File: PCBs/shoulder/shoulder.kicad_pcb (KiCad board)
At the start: 2 copper layers, 88 x 88 mm, 4 parts

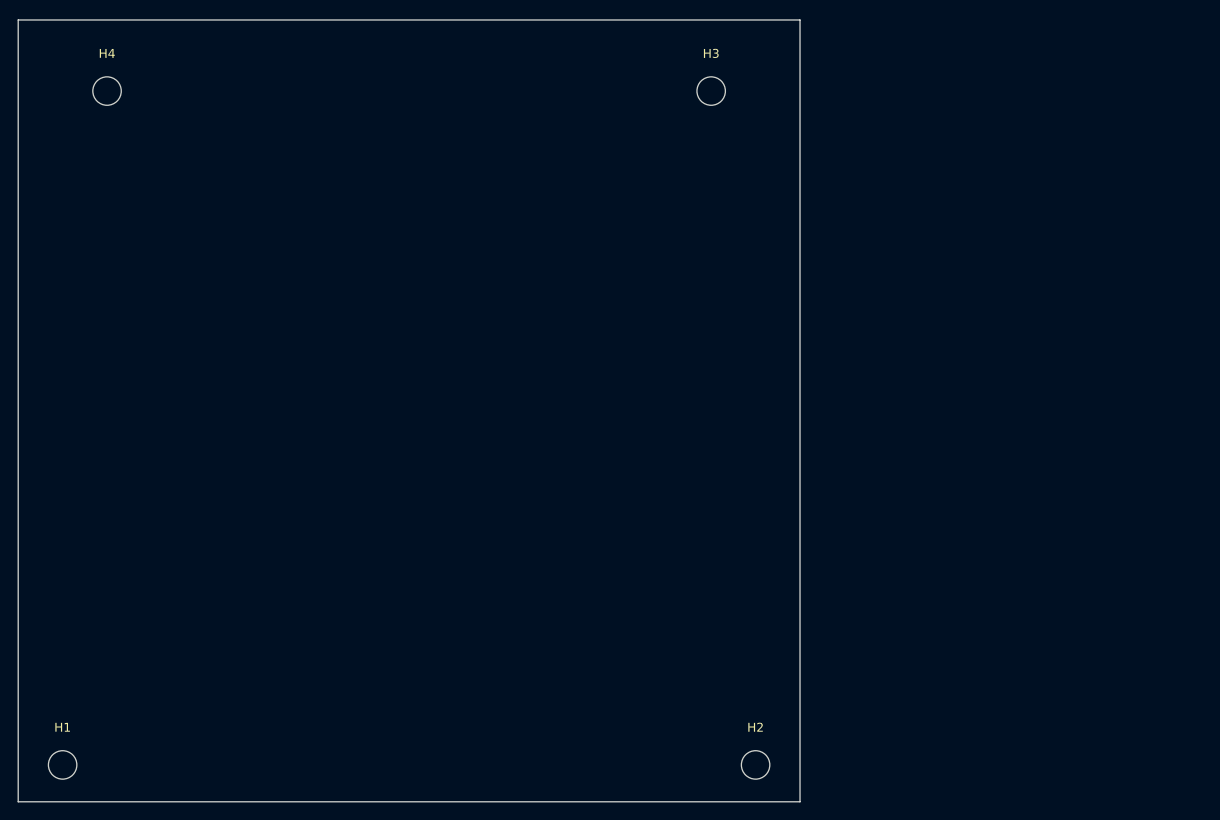
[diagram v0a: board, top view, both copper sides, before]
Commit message: Shoulder motor assy almost done. Need to find a library for the 2N551 NPN and redo the circuit. Ensure that the footprint pinout is correct
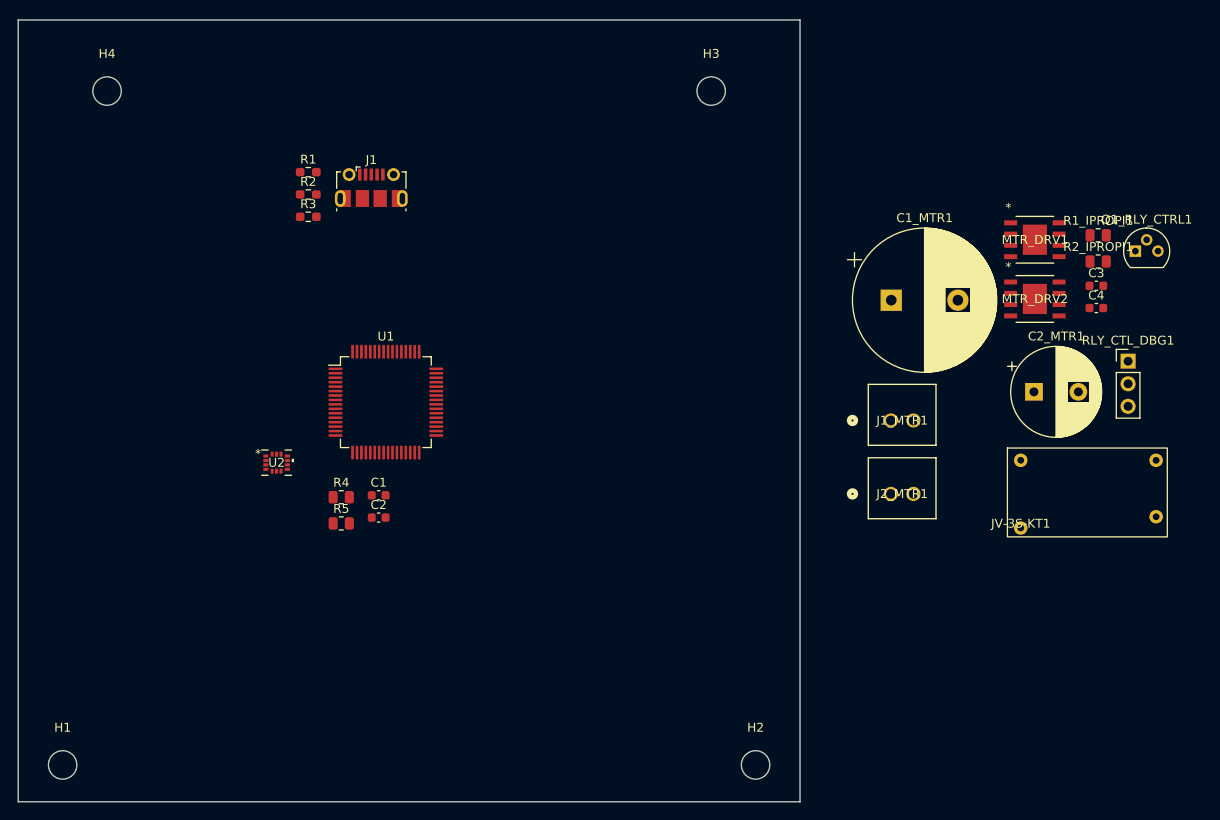
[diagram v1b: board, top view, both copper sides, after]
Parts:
- added C1: 100nF, Capacitor_SMD:C_0603_1608Metric, F.Cu at (97.1, 68.2)
- added C1_MTR1: 330muF, Capacitor_THT:CP_Radial_D16.0mm_P7.50mm, F.Cu at (154.8, 46.2)
- added C2: 100nF, Capacitor_SMD:C_0603_1608Metric, F.Cu at (97.1, 70.7)
- added C2_MTR1: 220muF, Capacitor_THT:CP_Radial_D10.0mm_P5.00mm, F.Cu at (170.9, 56.6)
- added C3: 100nF, Capacitor_SMD:C_0603_1608Metric, F.Cu at (177.9, 44.6)
- added C4: 100nF, Capacitor_SMD:C_0603_1608Metric, F.Cu at (177.9, 47.1)
- added J1: USB_B_Micro, Connector_USB:USB_Micro-B_Molex-105017-0001, F.Cu at (96.3, 33.6)
- added J1_MTR1: 705430001, 70543-0001:70543-0001_MOL, F.Cu at (154.8, 59.8)
- added J2_MTR1: 705430001, 70543-0001:70543-0001_MOL, F.Cu at (154.8, 68.0)
- added JV-3S-KT1: RELAY, JV-3S-KT:JV-3S-KT, F.Cu at (177.0, 66.8)
- added MTR_DRV1: DRV8251ADDAR, DRV8251A:SOIC8_DDA_TEX, F.Cu at (171.0, 39.4)
- added MTR_DRV2: DRV8251ADDAR, DRV8251A:SOIC8_DDA_TEX, F.Cu at (171.0, 46.1)
- added Q1_RLY_CTRL1: Q_NIGBT_CGE, Package_TO_SOT_THT:TO-92, F.Cu at (182.3, 40.7)
- added R1: 82k, Resistor_SMD:R_0603_1608Metric_Pad0.98x0.95mm_HandSolder, F.Cu at (89.2, 31.8)
- added R1_IPROPI1: 510Ohm, Resistor_SMD:R_0805_2012Metric, F.Cu at (178.1, 38.9)
- added R2: 33k, Resistor_SMD:R_0603_1608Metric_Pad0.98x0.95mm_HandSolder, F.Cu at (89.2, 34.3)
- added R2_IPROPI1: 510Ohm, Resistor_SMD:R_0805_2012Metric, F.Cu at (178.1, 41.9)
- added R3: 1k5, Resistor_SMD:R_0603_1608Metric_Pad0.98x0.95mm_HandSolder, F.Cu at (89.2, 36.9)
- added R4: 10k, Resistor_SMD:R_0805_2012Metric, F.Cu at (92.9, 68.4)
- added R5: 10k, Resistor_SMD:R_0805_2012Metric, F.Cu at (92.9, 71.4)
- added RLY_CTL_DBG1: Conn_01x03, Connector_PinHeader_2.54mm:PinHeader_1x03_P2.54mm_Vertical, F.Cu at (181.5, 53.1)
- added U1: STM32F303RETx, Package_QFP:LQFP-64_10x10mm_P0.5mm, F.Cu at (98.0, 57.7)
- added U2: LSM6DSMTR, LSM6DSMTR:LGA-14L_2P5X3X0P83_STM, F.Cu at (85.7, 64.5)

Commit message: Torso all but complete, making bogie before checking the last mark
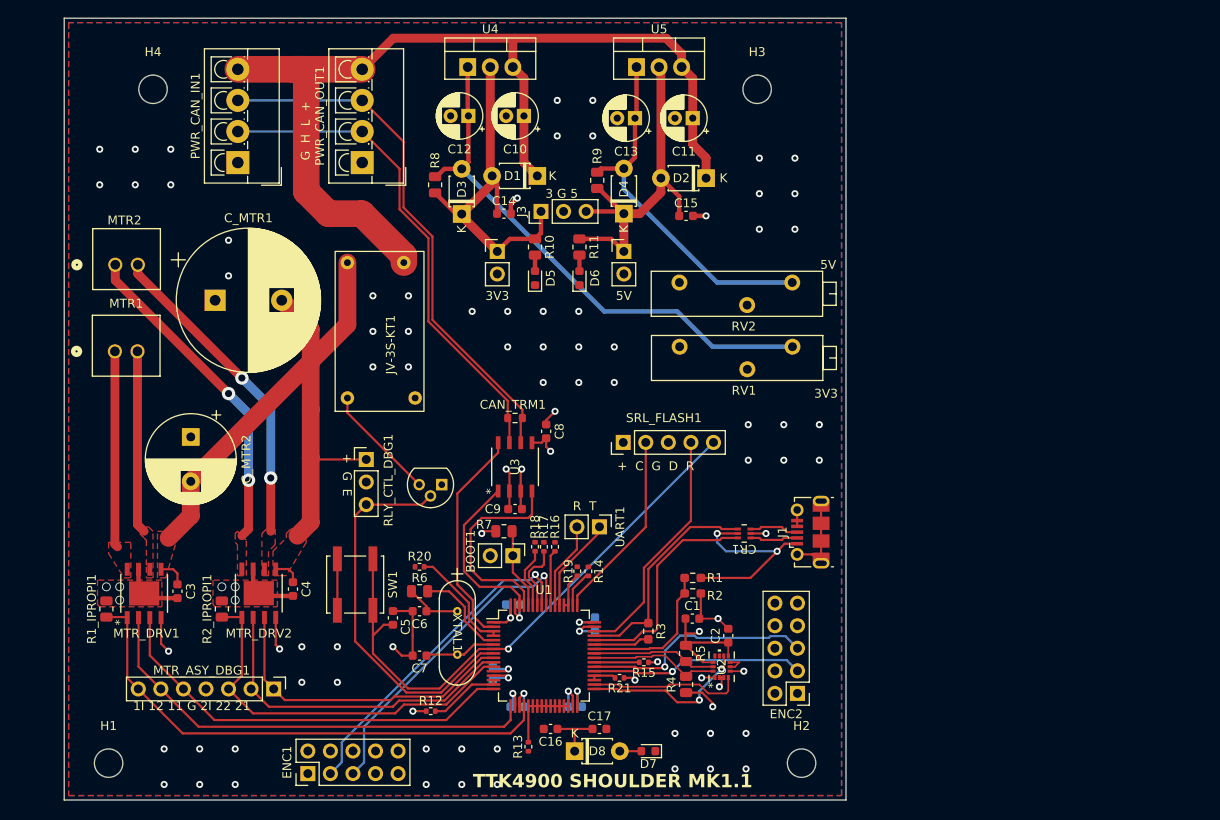
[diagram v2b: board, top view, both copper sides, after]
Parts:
- removed C1_MTR1: 330muF, Capacitor_THT:CP_Radial_D16.0mm_P7.50mm
- removed C2_MTR1: 220muF, Capacitor_THT:CP_Radial_D10.0mm_P5.00mm
- removed J1_MTR1, J2_MTR1: 705430001, 70543-0001:70543-0001_MOL
- added BOOT1: BOOTMODE, Connector_PinHeader_2.54mm:PinHeader_1x02_P2.54mm_Vertical, F.Cu at (112.2, 75.0)
- added C10: 10muF, Capacitor_THT:CP_Radial_D5.0mm_P2.00mm, F.Cu at (113.5, 25.5)
- added C11: 10muF, Capacitor_THT:CP_Radial_D5.0mm_P2.00mm, F.Cu at (132.5, 25.8)
- added C12: 10muF, Capacitor_THT:CP_Radial_D5.0mm_P2.00mm, F.Cu at (107.2, 25.5)
- added C13: 10muF, Capacitor_THT:CP_Radial_D5.0mm_P2.00mm, F.Cu at (126.0, 25.8)
- added C14: 100nF, Capacitor_SMD:C_0603_1608Metric, F.Cu at (111.2, 36.5)
- added C15: 100nF, Capacitor_SMD:C_0603_1608Metric, F.Cu at (131.8, 36.8)
- added C16: 4.7muF, Capacitor_SMD:C_0603_1608Metric, F.Cu at (116.5, 94.5)
- added C17: 1muF, Capacitor_SMD:C_0603_1608Metric, F.Cu at (122.0, 94.5)
- added C18: 10nF, Capacitor_SMD:C_0603_1608Metric, B.Cu at (110.0, 88.2)
- added C19: 100nF, Capacitor_SMD:C_0603_1608Metric, B.Cu at (112.2, 80.5)
- added C20: 100nF, Capacitor_SMD:C_0603_1608Metric, B.Cu at (121.5, 82.7)
- added C21: 100nF, Capacitor_SMD:C_0603_1608Metric, B.Cu at (119.2, 92.0)
- added C22: 100nF, Capacitor_SMD:C_0603_1608Metric, B.Cu at (112.8, 92.0)
- added C5: 100nF, Capacitor_SMD:C_0603_1608Metric, F.Cu at (98.8, 82.0)
- added C6: 20pF, Capacitor_SMD:C_0603_1608Metric, F.Cu at (101.8, 81.2)
- added C7: 20pF, Capacitor_SMD:C_0603_1608Metric, F.Cu at (101.8, 86.2)
- added C8: 100nF, Capacitor_SMD:C_0603_1608Metric, F.Cu at (116.0, 61.0)
- added C9: 100nF, Capacitor_SMD:C_0603_1608Metric, F.Cu at (112.5, 69.8)
- added CAN_TRM1: 120Ohm, Resistor_SMD:R_0603_1608Metric, F.Cu at (112.5, 59.5)
- added CR1: USBLC6-2P6, USBLC6:SOT-666_STM, F.Cu at (138.3, 72.5)
- added C_MTR1: 330muF, Capacitor_THT:CP_Radial_D16.0mm_P7.50mm, F.Cu at (78.7, 46.2)
- added C_MTR2: 220muF, Capacitor_THT:CP_Radial_D10.0mm_P5.00mm, F.Cu at (76.0, 61.6)
- added D1: IN4005, Diode_THT:D_T-1_P5.08mm_Horizontal, F.Cu at (115.0, 32.2)
- added D2: IN4005, Diode_THT:D_T-1_P5.08mm_Horizontal, F.Cu at (134.0, 32.5)
- added D3: IN4005, Diode_THT:D_T-1_P5.08mm_Horizontal, F.Cu at (106.5, 36.5)
- added D4: IN4005, Diode_THT:D_T-1_P5.08mm_Horizontal, F.Cu at (124.8, 36.5)
- added D5: LED_3V3, LED_SMD:LED_0603_1608Metric, F.Cu at (114.8, 43.8)
- added D6: LED_5V, LED_SMD:LED_0603_1608Metric, F.Cu at (119.8, 43.8)
- added D7: LED, LED_SMD:LED_0603_1608Metric, F.Cu at (127.5, 97.0)
- added D8: D_Zener, Diode_THT:D_T-1_P5.08mm_Horizontal, F.Cu at (119.2, 97.0)
- added ENC1: Conn_02x05_Odd_Even, Connector_PinHeader_2.54mm:PinHeader_2x05_P2.54mm_Vertical, F.Cu at (89.2, 99.5)
- added ENC2: Conn_02x05_Odd_Even, Connector_PinHeader_2.54mm:PinHeader_2x05_P2.54mm_Vertical, F.Cu at (144.3, 90.5)
- added J2: Conn_01x07, Connector_PinHeader_2.54mm:PinHeader_1x07_P2.54mm_Vertical, F.Cu at (85.3, 90.0)
- added J3: Conn_01x03, Connector_PinHeader_2.54mm:PinHeader_1x03_P2.54mm_Vertical, F.Cu at (115.4, 36.2)
- added JP1: Jumper_2_Open, Connector_PinHeader_2.54mm:PinHeader_1x02_P2.54mm_Vertical, F.Cu at (110.5, 40.8)
- added JP2: Jumper_2_Open, Connector_PinHeader_2.54mm:PinHeader_1x02_P2.54mm_Vertical, F.Cu at (124.8, 40.8)
- added MTR1: 705430001, 70543-0001:70543-0001_MOL, F.Cu at (67.5, 52.0)
- added MTR2: 705430001, 70543-0001:70543-0001_MOL, F.Cu at (67.5, 42.2)
- added PWR_CAN_IN1: Conn_01x04, TerminalBlock_4Ucon:TerminalBlock_4Ucon_1x04_P3.50mm_Vertical, F.Cu at (81.3, 30.8)
- added PWR_CAN_OUT1: Conn_01x04, TerminalBlock_4Ucon:TerminalBlock_4Ucon_1x04_P3.50mm_Vertical, F.Cu at (95.3, 30.8)
- added R10: 1k5, Resistor_SMD:R_0805_2012Metric, F.Cu at (114.8, 40.2)
- added R11: 1k5, Resistor_SMD:R_0805_2012Metric, F.Cu at (119.8, 40.2)
- added R12: 40kOhm, Resistor_SMD:R_0402_1005Metric, F.Cu at (103.0, 92.5)
- added R13: 40kOhm, Resistor_SMD:R_0402_1005Metric, F.Cu at (114.0, 96.5)
- added R14: 40kOhm, Resistor_SMD:R_0402_1005Metric, F.Cu at (120.8, 76.8)
- added R15: 40kOhm, Resistor_SMD:R_0402_1005Metric, F.Cu at (127.0, 87.0)
- added R16: 40kOhm, Resistor_SMD:R_0402_1005Metric, F.Cu at (117.0, 74.0)
- added R17: 40kOhm, Resistor_SMD:R_0402_1005Metric, F.Cu at (115.8, 74.0)
- added R18: 40kOhm, Resistor_SMD:R_0402_1005Metric, F.Cu at (114.8, 74.0)
- added R19: 40kOhm, Resistor_SMD:R_0402_1005Metric, F.Cu at (119.5, 76.8)
- added R20: 40kOhm, Resistor_SMD:R_0402_1005Metric, F.Cu at (101.8, 76.2)
- added R21: 40kOhm, Resistor_SMD:R_0402_1005Metric, F.Cu at (124.3, 88.8)
- added R6: 340Ohm, Resistor_SMD:R_0805_2012Metric, F.Cu at (101.8, 79.0)
- added R7: 10kOhm, Resistor_SMD:R_0805_2012Metric, F.Cu at (111.2, 72.2)
- added R8: 240Ohm, Resistor_SMD:R_0805_2012Metric, F.Cu at (103.5, 33.2)
- added R9: 240Ohm, Resistor_SMD:R_0805_2012Metric, F.Cu at (121.8, 32.8)
- added RV1: 0,386k, Potentiometer_THT:Potentiometer_Bourns_3006P_Horizontal, F.Cu at (131.0, 51.5)
- added RV2: 0,706k, Potentiometer_THT:Potentiometer_Bourns_3006P_Horizontal, F.Cu at (131.0, 44.2)
- added SRL_FLASH1: Conn_01x05, Connector_PinHeader_2.54mm:PinHeader_1x05_P2.54mm_Vertical, F.Cu at (124.7, 62.2)
- added SW1: RESET, Button_Switch_SMD:SW_Push_1P1T_NO_CK_KSC6xxJ, F.Cu at (94.5, 78.2)
- added U3: TJA1057GT/3J, TJA1057BT:SOT96-1_SO8_NXP, F.Cu at (112.5, 65.0)
- added U4: LM317_TO-220, Package_TO_SOT_THT:TO-220-3_Vertical, F.Cu at (107.2, 20.0)
- added U5: LM317_TO-220, Package_TO_SOT_THT:TO-220-3_Vertical, F.Cu at (126.2, 20.0)
- added UART1: Conn_01x02, Connector_PinHeader_2.54mm:PinHeader_1x02_P2.54mm_Vertical, F.Cu at (122.0, 71.8)
- added XTAL1: ABL-16.000MHZ-B2, ABL-16.000MHZ-B1U-T:XTAL_ABL-16_ABR, F.Cu at (106.0, 81.2)
- moved R1_IPROPI1 119.3 mm to (66.5, 81.0), turned to 90 degrees
- moved C3 109.0 mm to (74.5, 79.0), turned to 90 degrees
- moved MTR_DRV1 107.9 mm to (70.8, 79.2), turned to 90 degrees
- moved R2_IPROPI1 106.1 mm to (79.5, 81.0), turned to 90 degrees
- moved C4 95.8 mm to (87.5, 78.8), turned to 90 degrees
- moved MTR_DRV2 93.4 mm to (83.7, 79.2), turned to 90 degrees
- moved RLY_CTL_DBG1 86.5 mm to (95.8, 64.2)
- moved JV-3S-KT1 82.7 mm to (96.2, 49.6), turned to 90 degrees
- moved Q1_RLY_CTRL1 82.4 mm to (104.2, 67.0), turned to 180 degrees
- moved R1 62.9 mm to (132.5, 77.5), turned to 180 degrees
- moved J1 62.8 mm to (145.7, 72.3), turned to 90 degrees
- moved R2 62.4 mm to (132.5, 79.2)
- moved R3 60.3 mm to (127.5, 83.5), turned to -90 degrees
- moved U2 55.1 mm to (135.8, 87.5), turned to 90 degrees
- moved R4 44.2 mm to (131.8, 89.5), turned to 90 degrees
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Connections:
- J1 pad 2: /USB_assy/DM -> Net-(J1-D-)
- J1 pad 3: /USB_assy/DP -> Net-(J1-D+)
- J1 pad 4: /USB_assy/Ground -> GND
- J1 pad 5: /USB_assy/Ground -> GND
- J1 pad 6: /USB_assy/Ground -> GND
- MTR_DRV1 pad 1: /Motor_assy/DRV1_IPROPI -> /DRV1_IPROPI
- MTR_DRV1 pad 2: /Motor_assy/DRV1_IN2 -> /DRV1_IN2
- MTR_DRV1 pad 3: /Motor_assy/DRV1_IN1 -> /DRV1_IN1
- MTR_DRV2 pad 1: /Motor_assy/DRV2_IPROPI -> /DRV2_IPROPI
- MTR_DRV2 pad 2: /Motor_assy/DRV2_IN2 -> /DRV2_IN2
- MTR_DRV2 pad 3: /Motor_assy/DRV2_IN1 -> /DRV2_IN1
- Q1_RLY_CTRL1 pad 2: /Motor_assy/RELAY_EN -> /RELAY_EN
- R1 pad 2: /USB_assy/VBUS -> /USB_VBUS
- R1_IPROPI1 pad 1: /Motor_assy/DRV1_IPROPI -> /DRV1_IPROPI
- R2 pad 1: /USB_assy/VBUS -> /USB_VBUS
- R2 pad 2: /USB_assy/Ground -> GND
- R2_IPROPI1 pad 1: /Motor_assy/DRV2_IPROPI -> /DRV2_IPROPI
- R3 pad 1: /USB_assy/DP -> /USB_DP
- R3 pad 2: /USB_assy/DP_DRV -> /USB_DP_DRV
- R4 pad 2: /IMU_assy/SDA -> /I2C_SDA
- R5 pad 2: /IMU_assy/SCL -> /I2C_SCL
- RLY_CTL_DBG1 pad 3: /Motor_assy/RELAY_EN -> /RELAY_EN
- U1 pad 1: unconnected-(U1-VBAT-Pad1) -> +3V3
- U1 pad 10: unconnected-(U1-PC2-Pad10) -> /DRV2_IN2
- U1 pad 11: unconnected-(U1-PC3-Pad11) -> /DRV2_IPROPI
- U1 pad 12: unconnected-(U1-VSSA-Pad12) -> GND
- U1 pad 13: unconnected-(U1-VDDA-Pad13) -> +3V3
- U1 pad 14: unconnected-(U1-PA0-Pad14) -> Net-(U1-PA0)
- U1 pad 15: unconnected-(U1-PA1-Pad15) -> Net-(U1-PA0)
- U1 pad 16: unconnected-(U1-PA2-Pad16) -> /DRV1_IN1
- U1 pad 17: unconnected-(U1-PA3-Pad17) -> /DRV1_IN2
- U1 pad 18: Net-(U1-VSS-Pad18) -> GND
- U1 pad 19: unconnected-(U1-VDD-Pad19) -> +3V3
- U1 pad 2: unconnected-(U1-PC13-Pad2) -> /CAN_EN
- U1 pad 20: unconnected-(U1-PA4-Pad20) -> /DRV1_IPROPI
- U1 pad 21: unconnected-(U1-PA5-Pad21) -> /GND_RES1
- U1 pad 22: unconnected-(U1-PA6-Pad22) -> /GND_RES1
- U1 pad 23: unconnected-(U1-PA7-Pad23) -> /GND_RES1
- U1 pad 24: unconnected-(U1-PC4-Pad24) -> /GND_RES1
- U1 pad 25: unconnected-(U1-PC5-Pad25) -> /GND_RES1
- U1 pad 26: unconnected-(U1-PB0-Pad26) -> /GND_RES1
- U1 pad 27: unconnected-(U1-PB1-Pad27) -> /GND_RES1
- U1 pad 28: unconnected-(U1-PB2-Pad28) -> /GND_RES1
- U1 pad 29: unconnected-(U1-PB10-Pad29) -> /GND_RES1
- U1 pad 3: unconnected-(U1-PC14-Pad3) -> Net-(U1-PC14)
- U1 pad 30: unconnected-(U1-PB11-Pad30) -> /GND_RES1
- U1 pad 31: Net-(U1-VSS-Pad18) -> GND
- U1 pad 32: unconnected-(U1-VDD-Pad32) -> +3V3
- U1 pad 33: unconnected-(U1-PB12-Pad33) -> /IMU_IN2
- U1 pad 34: unconnected-(U1-PB13-Pad34) -> /IMU_INT1
- U1 pad 35: unconnected-(U1-PB14-Pad35) -> Net-(U1-PB14)
- U1 pad 36: unconnected-(U1-PB15-Pad36) -> Net-(U1-PB14)
- U1 pad 37: unconnected-(U1-PC6-Pad37) -> /ENC2B
- U1 pad 38: unconnected-(U1-PC7-Pad38) -> /ENC2A
- U1 pad 39: unconnected-(U1-PC8-Pad39) -> Net-(U1-PC8)
- U1 pad 4: unconnected-(U1-PC15-Pad4) -> Net-(U1-PC14)
- U1 pad 40: unconnected-(U1-PC9-Pad40) -> /I2C_SDA
- U1 pad 41: unconnected-(U1-PA8-Pad41) -> /I2C_SCL
- U1 pad 42: unconnected-(U1-PA9-Pad42) -> /USB_VBUS
- U1 pad 43: unconnected-(U1-PA10-Pad43) -> /USB_DP_DRV
- U1 pad 44: unconnected-(U1-PA11-Pad44) -> /USB_DM
- U1 pad 45: unconnected-(U1-PA12-Pad45) -> /USB_DP
- U1 pad 46: unconnected-(U1-PA13-Pad46) -> /FLASH_DIO
- U1 pad 47: Net-(U1-VSS-Pad18) -> GND
- U1 pad 48: unconnected-(U1-VDD-Pad48) -> +3V3
- U1 pad 49: unconnected-(U1-PA14-Pad49) -> /FLASH_CLK
- U1 pad 5: unconnected-(U1-PF0-Pad5) -> /OSC_IN
- U1 pad 50: unconnected-(U1-PA15-Pad50) -> Net-(U1-PA15)
- U1 pad 51: unconnected-(U1-PC10-Pad51) -> Net-(U1-PC10)
- U1 pad 52: unconnected-(U1-PC11-Pad52) -> Net-(U1-PC10)
- U1 pad 53: unconnected-(U1-PC12-Pad53) -> /UART_TX
- U1 pad 54: unconnected-(U1-PD2-Pad54) -> /UART_RX
- U1 pad 55: unconnected-(U1-PB3-Pad55) -> Net-(U1-PB3)
- U1 pad 56: unconnected-(U1-PB4-Pad56) -> /ENC1A
- U1 pad 57: unconnected-(U1-PB5-Pad57) -> /ENC1B
- U1 pad 58: unconnected-(U1-PB6-Pad58) -> Net-(U1-PB6)
- U1 pad 59: unconnected-(U1-PB7-Pad59) -> Net-(U1-PB7)
- U1 pad 6: unconnected-(U1-PF1-Pad6) -> /OSC_OUT
- U1 pad 60: unconnected-(U1-BOOT0-Pad60) -> /BOOT0
- U1 pad 61: unconnected-(U1-PB8-Pad61) -> /CAN_RX
- U1 pad 62: unconnected-(U1-PB9-Pad62) -> /CAN_TX
- U1 pad 63: Net-(U1-VSS-Pad18) -> GND
- U1 pad 64: unconnected-(U1-VDD-Pad64) -> +3V3
- U1 pad 7: unconnected-(U1-NRST-Pad7) -> /RESET
- U1 pad 8: unconnected-(U1-PC0-Pad8) -> /RELAY_EN
- U1 pad 9: unconnected-(U1-PC1-Pad9) -> /DRV2_IN1
- U2 pad 13: /IMU_assy/SCL -> /I2C_SCL
- U2 pad 14: /IMU_assy/SDA -> /I2C_SDA
- U2 pad 4: /IMU_assy/INT1 -> /IMU_INT1
- U2 pad 9: /IMU_assy/INT2 -> /IMU_IN2
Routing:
- net +48V: track 0.00 -> 114.0 mm
- net GND: track 0.00 -> 86.1 mm, vias 0 -> 88
- net Net-(JV-3S-KT1-COM): track 0.00 -> 80.5 mm
- net /RESET: track 0.00 -> 64.9 mm, vias 0 -> 1
- net Net-(D3-A): track 0.00 -> 60.7 mm
- net /CANL: track 0.00 -> 60.1 mm
- net +3V3: track 0.00 -> 59.2 mm, vias 0 -> 12
- net /DRV1_IPROPI: track 0.00 -> 58.6 mm
- net /CANH: track 0.00 -> 55.9 mm
- net /DRV1_IN2: track 0.00 -> 52.1 mm
- net /DRV1_IN1: track 0.00 -> 47.4 mm
- net /DRV2_IPROPI: track 0.00 -> 44.1 mm
- net /RELAY_EN: track 0.00 -> 43.3 mm
- net Net-(D2-A): track 0.00 -> 42.8 mm
- net Net-(D4-A): track 0.00 -> 40.8 mm
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- added copper zone on In2.Cu, net +3V3
- added copper zone on B.Cu, net +5V
- added copper zone on F.Cu, net GND
- added copper zone on In1.Cu, net GND
- added copper zone on F.Cu, net Net-(JV-3S-KT1-COM)
- added copper zone on F.Cu, net Net-(MTR1-IN)
- added copper zone on F.Cu, net Net-(MTR1-OUT)
- added copper zone on F.Cu, net Net-(MTR2-IN)
- added copper zone on F.Cu, net Net-(MTR2-OUT)
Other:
- copper layers 2 -> 4
- board text added: "+ C G D R"
- board text added: "+ G E"
- board text added: "1I 12 11 G 2I 22 21"
- board text added: "3 G 5"
- board text added: "3V3"
- board text added: "5V"
- board text added: "G H L +"
- board text added: "KRISTIAN BLOM"
- board text added: "MTR_ASY_DBG1"
- board text added: "R T"
- board text added: "TTK4900 SHOULDER MK1.1"
